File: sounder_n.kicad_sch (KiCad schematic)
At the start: 20 parts

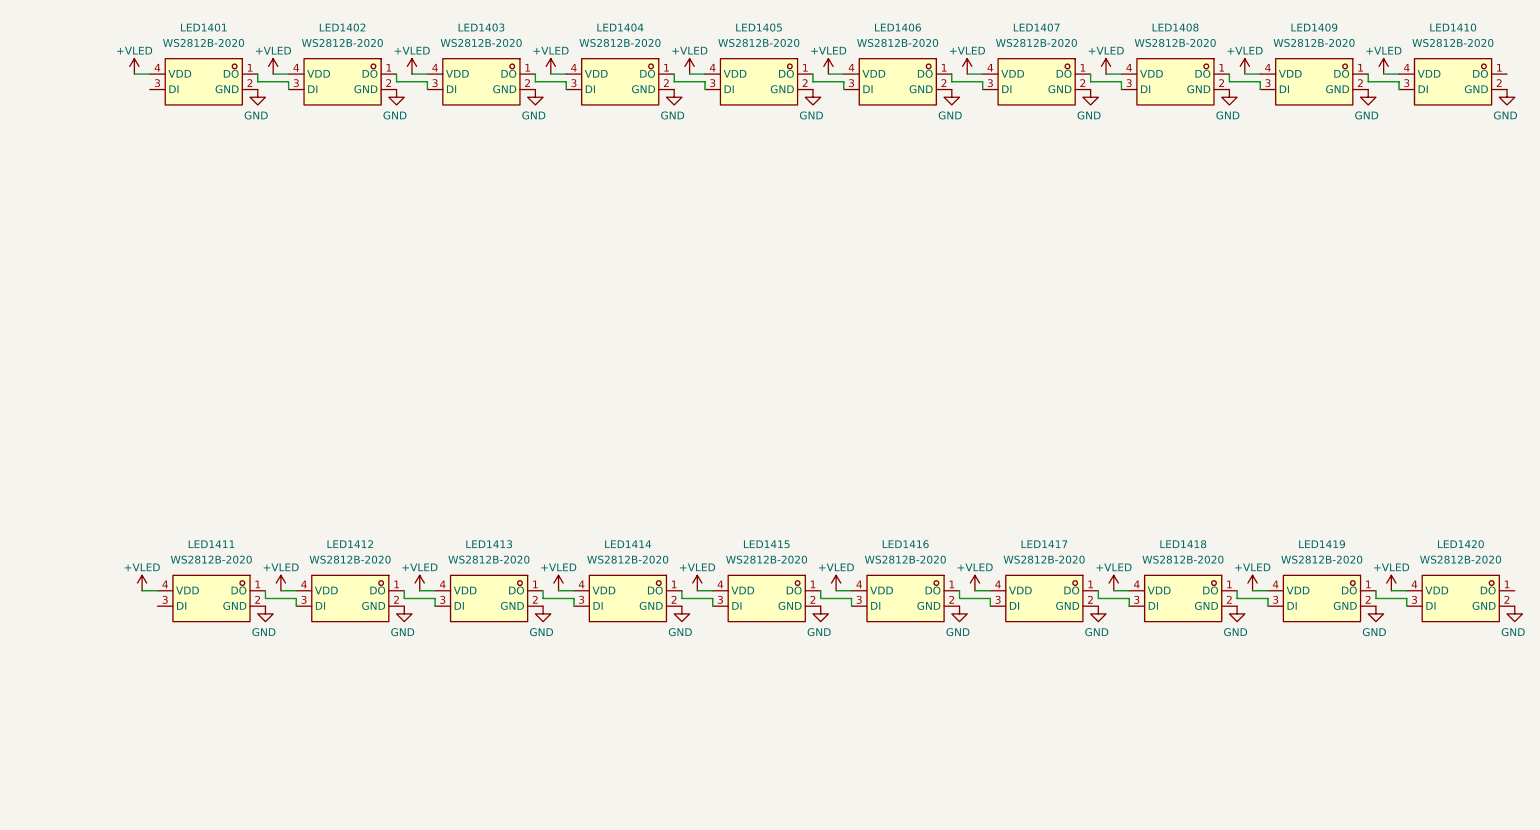
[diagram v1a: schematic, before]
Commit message: Initial LED placement complete
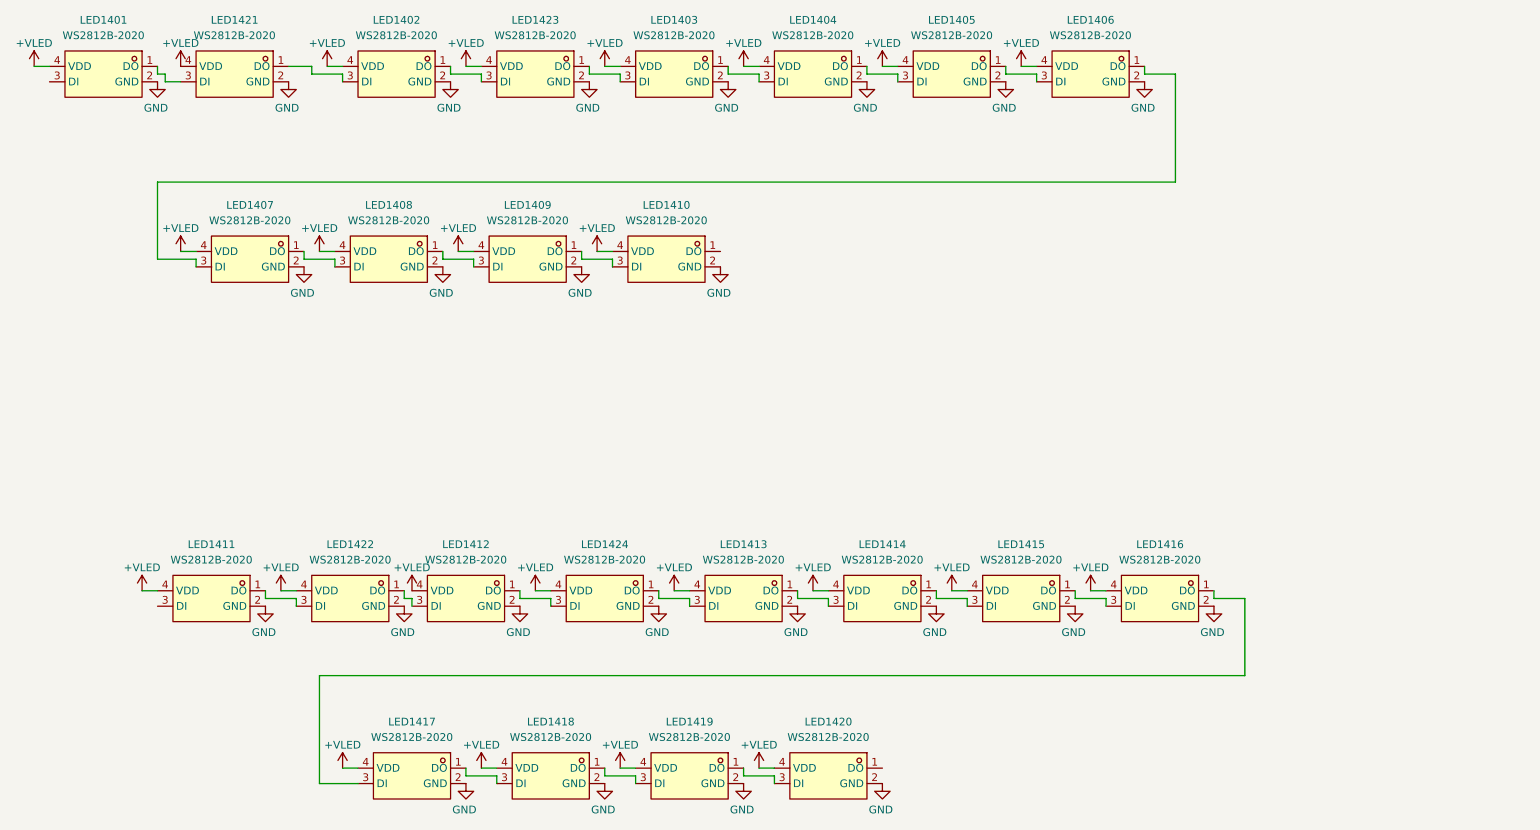
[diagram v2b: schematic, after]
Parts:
- added LED1421, LED1422, LED1423, LED1424: WS2812B-2020, EasyEDA:LED-SMD_4P-L2.0-W2.0-TL_WS2812B-2020, symbol EasyEDA:WS2812B-2020
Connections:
- net +VLED: now also LED1421.4 (VDD), LED1422.4 (VDD), LED1423.4 (VDD), LED1424.4 (VDD)
- net GND: now also LED1421.2 (GND), LED1422.2 (GND), LED1423.2 (GND), LED1424.2 (GND)
- net at LED1411.1 (DO): now also LED1422.3 (DI); no longer LED1412.3 (DI)
- net at LED1403.3 (DI): now also LED1423.1 (DO); no longer LED1402.1 (DO)
- net at LED1412.1 (DO): now also LED1424.3 (DI); no longer LED1413.3 (DI)
- net at LED1401.1 (DO): now also LED1421.3 (DI); no longer LED1402.3 (DI)
- new net: LED1412.3 (DI), LED1422.1 (DO)
- new net: LED1402.3 (DI), LED1421.1 (DO)
- new net: LED1413.3 (DI), LED1424.1 (DO)
- new net: LED1402.1 (DO), LED1423.3 (DI)
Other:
- moved on the sheet: LED1402, LED1403, LED1404, LED1405, LED1406

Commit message: Add rail labels
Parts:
- renumbered LED1421 to LED1402, LED1402 to LED1403, LED1423 to LED1404, LED1403 to LED1405, LED1404 to LED1406, LED1405 to LED1407, LED1406 to LED1408, LED1407 to LED1409, LED1408 to LED1410, LED1409 to LED1411, LED1410 to LED1412, LED1411 to LED1413, LED1422 to LED1414, LED1412 to LED1415, LED1424 to LED1416, LED1413 to LED1417, LED1414 to LED1418, LED1415 to LED1419, LED1416 to LED1420, LED1417 to LED1421, LED1418 to LED1422, LED1419 to LED1423, LED1420 to LED1424
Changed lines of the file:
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@@
 		(in_pos_files yes)
 		(dnp no)
-		(property "Reference" "LED1410"
+		(property "Reference" "LED1412"
 			(at 120.65 50.8 0)
 			(show_name no)
@@
 			(project "transit"
 				(path "/3763eade-a8c8-4ec0-9cf2-9db4442b4ee5/77ee1b5c-3800-46a1-aec6-a1e3c1d3f80f/996df8f8-04d4-4bb4-8f37-9760745edbe2"
-					(reference "LED1410")
+					(reference "LED1412")
 					(unit 1)
 				)
@@
 		(in_pos_files yes)
 		(dnp no)
-		(property "Reference" "LED1411"
+		(property "Reference" "LED1413"
 			(at 45.72 106.68 0)
 			(show_name no)
@@
 			(project "transit"
 				(path "/3763eade-a8c8-4ec0-9cf2-9db4442b4ee5/77ee1b5c-3800-46a1-aec6-a1e3c1d3f80f/996df8f8-04d4-4bb4-8f37-9760745edbe2"
-					(reference "LED1411")
+					(reference "LED1413")
 					(unit 1)
 				)
@@
 		(in_pos_files yes)
 		(dnp no)
-		(property "Reference" "LED1403"
+		(property "Reference" "LED1405"
 			(at 121.92 20.32 0)
 			(show_name no)
@@
 			(project "transit"
 				(path "/3763eade-a8c8-4ec0-9cf2-9db4442b4ee5/77ee1b5c-3800-46a1-aec6-a1e3c1d3f80f/996df8f8-04d4-4bb4-8f37-9760745edbe2"
-					(reference "LED1403")
+					(reference "LED1405")
 					(unit 1)
 				)
@@
 		(in_pos_files yes)
 		(dnp no)
-		(property "Reference" "LED1404"
+		(property "Reference" "LED1406"
 			(at 144.78 20.32 0)
 			(show_name no)
@@
 			(project "transit"
 				(path "/3763eade-a8c8-4ec0-9cf2-9db4442b4ee5/77ee1b5c-3800-46a1-aec6-a1e3c1d3f80f/996df8f8-04d4-4bb4-8f37-9760745edbe2"
-					(reference "LED1404")
+					(reference "LED1406")
 					(unit 1)
 				)
@@
 		(in_pos_files yes)
 		(dnp no)
-		(property "Reference" "LED1414"
+		(property "Reference" "LED1418"
 			(at 156.21 106.68 0)
 			(show_name no)
@@
 			(project "transit"
 				(path "/3763eade-a8c8-4ec0-9cf2-9db4442b4ee5/77ee1b5c-3800-46a1-aec6-a1e3c1d3f80f/996df8f8-04d4-4bb4-8f37-9760745edbe2"
-					(reference "LED1414")
+					(reference "LED1418")
 					(unit 1)
 				)
@@
 		(in_pos_files yes)
 		(dnp no)
-		(property "Reference" "LED1422"
+		(property "Reference" "LED1414"
 			(at 68.58 106.68 0)
 			(show_name no)
@@
 			(project "transit"
 				(path "/3763eade-a8c8-4ec0-9cf2-9db4442b4ee5/77ee1b5c-3800-46a1-aec6-a1e3c1d3f80f/996df8f8-04d4-4bb4-8f37-9760745edbe2"
-					(reference "LED1422")
+					(reference "LED1414")
 					(unit 1)
 				)
@@
 		(in_pos_files yes)
 		(dnp no)
-		(property "Reference" "LED1405"
+		(property "Reference" "LED1407"
 			(at 167.64 20.32 0)
 			(show_name no)
@@
 			(project "transit"
 				(path "/3763eade-a8c8-4ec0-9cf2-9db4442b4ee5/77ee1b5c-3800-46a1-aec6-a1e3c1d3f80f/996df8f8-04d4-4bb4-8f37-9760745edbe2"
-					(reference "LED1405")
+					(reference "LED1407")
 					(unit 1)
 				)
@@
 		(in_pos_files yes)
 		(dnp no)
-		(property "Reference" "LED1408"
+		(property "Reference" "LED1410"
 			(at 74.93 50.8 0)
 			(show_name no)
@@
 			(project "transit"
 				(path "/3763eade-a8c8-4ec0-9cf2-9db4442b4ee5/77ee1b5c-3800-46a1-aec6-a1e3c1d3f80f/996df8f8-04d4-4bb4-8f37-9760745edbe2"
-					(reference "LED1408")
+					(reference "LED1410")
 					(unit 1)
 				)
@@
 		(in_pos_files yes)
 		(dnp no)
-		(property "Reference" "LED1416"
+		(property "Reference" "LED1420"
 			(at 201.93 106.68 0)
 			(show_name no)
@@
 			(project "transit"
 				(path "/3763eade-a8c8-4ec0-9cf2-9db4442b4ee5/77ee1b5c-3800-46a1-aec6-a1e3c1d3f80f/996df8f8-04d4-4bb4-8f37-9760745edbe2"
-					(reference "LED1416")
+					(reference "LED1420")
 					(unit 1)
 				)
@@
 		(in_pos_files yes)
 		(dnp no)
-		(property "Reference" "LED1415"
+		(property "Reference" "LED1419"
 			(at 179.07 106.68 0)
 			(show_name no)
@@
 			(project "transit"
 				(path "/3763eade-a8c8-4ec0-9cf2-9db4442b4ee5/77ee1b5c-3800-46a1-aec6-a1e3c1d3f80f/996df8f8-04d4-4bb4-8f37-9760745edbe2"
-					(reference "LED1415")
+					(reference "LED1419")
 					(unit 1)
 				)
@@
 		(in_pos_files yes)
 		(dnp no)
-		(property "Reference" "LED1406"
+		(property "Reference" "LED1408"
 			(at 190.5 20.32 0)
 			(show_name no)
@@
 			(project "transit"
 				(path "/3763eade-a8c8-4ec0-9cf2-9db4442b4ee5/77ee1b5c-3800-46a1-aec6-a1e3c1d3f80f/996df8f8-04d4-4bb4-8f37-9760745edbe2"
-					(reference "LED1406")
+					(reference "LED1408")
 					(unit 1)
 				)
@@
 		(in_pos_files yes)
 		(dnp no)
-		(property "Reference" "LED1412"
+		(property "Reference" "LED1415"
 			(at 87.63 106.68 0)
 			(show_name no)
@@
 			(project "transit"
 				(path "/3763eade-a8c8-4ec0-9cf2-9db4442b4ee5/77ee1b5c-3800-46a1-aec6-a1e3c1d3f80f/996df8f8-04d4-4bb4-8f37-9760745edbe2"
-					(reference "LED1412")
+					(reference "LED1415")
 					(unit 1)
 				)
@@
 		(in_pos_files yes)
 		(dnp no)
-		(property "Reference" "LED1421"
+		(property "Reference" "LED1402"
 			(at 49.53 20.32 0)
 			(show_name no)
@@
 			(project "transit"
 				(path "/3763eade-a8c8-4ec0-9cf2-9db4442b4ee5/77ee1b5c-3800-46a1-aec6-a1e3c1d3f80f/996df8f8-04d4-4bb4-8f37-9760745edbe2"
-					(reference "LED1421")
+					(reference "LED1402")
 					(unit 1)
 				)
@@
 		(in_pos_files yes)
 		(dnp no)
-		(property "Reference" "LED1418"
+		(property "Reference" "LED1422"
 			(at 101.6 135.89 0)
 			(show_name no)
@@
 			(project "transit"
 				(path "/3763eade-a8c8-4ec0-9cf2-9db4442b4ee5/77ee1b5c-3800-46a1-aec6-a1e3c1d3f80f/996df8f8-04d4-4bb4-8f37-9760745edbe2"
-					(reference "LED1418")
+					(reference "LED1422")
 					(unit 1)
 				)
@@
 		(in_pos_files yes)
 		(dnp no)
-		(property "Reference" "LED1420"
+		(property "Reference" "LED1424"
 			(at 147.32 135.89 0)
 			(show_name no)
@@
 			(project "transit"
 				(path "/3763eade-a8c8-4ec0-9cf2-9db4442b4ee5/77ee1b5c-3800-46a1-aec6-a1e3c1d3f80f/996df8f8-04d4-4bb4-8f37-9760745edbe2"
-					(reference "LED1420")
+					(reference "LED1424")
 					(unit 1)
 				)
@@
 		(in_pos_files yes)
 		(dnp no)
-		(property "Reference" "LED1417"
+		(property "Reference" "LED1421"
 			(at 78.74 135.89 0)
 			(show_name no)
@@
 			(project "transit"
 				(path "/3763eade-a8c8-4ec0-9cf2-9db4442b4ee5/77ee1b5c-3800-46a1-aec6-a1e3c1d3f80f/996df8f8-04d4-4bb4-8f37-9760745edbe2"
-					(reference "LED1417")
+					(reference "LED1421")
 					(unit 1)
 				)
@@
 		(in_pos_files yes)
 		(dnp no)
-		(property "Reference" "LED1419"
+		(property "Reference" "LED1423"
 			(at 124.46 135.89 0)
 			(show_name no)
@@
 			(project "transit"
 				(path "/3763eade-a8c8-4ec0-9cf2-9db4442b4ee5/77ee1b5c-3800-46a1-aec6-a1e3c1d3f80f/996df8f8-04d4-4bb4-8f37-9760745edbe2"
-					(reference "LED1419")
+					(reference "LED1423")
 					(unit 1)
 				)
@@
 		(in_pos_files yes)
 		(dnp no)
-		(property "Reference" "LED1413"
+		(property "Reference" "LED1417"
 			(at 133.35 106.68 0)
 			(show_name no)
@@
 			(project "transit"
 				(path "/3763eade-a8c8-4ec0-9cf2-9db4442b4ee5/77ee1b5c-3800-46a1-aec6-a1e3c1d3f80f/996df8f8-04d4-4bb4-8f37-9760745edbe2"
-					(reference "LED1413")
+					(reference "LED1417")
 					(unit 1)
 				)
@@
 		(in_pos_files yes)
 		(dnp no)
-		(property "Reference" "LED1407"
+		(property "Reference" "LED1409"
 			(at 52.07 50.8 0)
 			(show_name no)
@@
 			(project "transit"
 				(path "/3763eade-a8c8-4ec0-9cf2-9db4442b4ee5/77ee1b5c-3800-46a1-aec6-a1e3c1d3f80f/996df8f8-04d4-4bb4-8f37-9760745edbe2"
-					(reference "LED1407")
+					(reference "LED1409")
 					(unit 1)
 				)
@@
 		(in_pos_files yes)
 		(dnp no)
-		(property "Reference" "LED1409"
+		(property "Reference" "LED1411"
 			(at 97.79 50.8 0)
 			(show_name no)
@@
 			(project "transit"
 				(path "/3763eade-a8c8-4ec0-9cf2-9db4442b4ee5/77ee1b5c-3800-46a1-aec6-a1e3c1d3f80f/996df8f8-04d4-4bb4-8f37-9760745edbe2"
-					(reference "LED1409")
+					(reference "LED1411")
 					(unit 1)
 				)
@@
 		(in_pos_files yes)
 		(dnp no)
-		(property "Reference" "LED1402"
+		(property "Reference" "LED1403"
 			(at 76.2 20.32 0)
 			(show_name no)
@@
 			(project "transit"
 				(path "/3763eade-a8c8-4ec0-9cf2-9db4442b4ee5/77ee1b5c-3800-46a1-aec6-a1e3c1d3f80f/996df8f8-04d4-4bb4-8f37-9760745edbe2"
-					(reference "LED1402")
+					(reference "LED1403")
 					(unit 1)
 				)
@@
 		(in_pos_files yes)
 		(dnp no)
-		(property "Reference" "LED1423"
+		(property "Reference" "LED1404"
 			(at 99.06 20.32 0)
 			(show_name no)
@@
 			(project "transit"
 				(path "/3763eade-a8c8-4ec0-9cf2-9db4442b4ee5/77ee1b5c-3800-46a1-aec6-a1e3c1d3f80f/996df8f8-04d4-4bb4-8f37-9760745edbe2"
-					(reference "LED1423")
+					(reference "LED1404")
 					(unit 1)
 				)
@@
 		(in_pos_files yes)
 		(dnp no)
-		(property "Reference" "LED1424"
+		(property "Reference" "LED1416"
 			(at 110.49 106.68 0)
 			(show_name no)
@@
 			(project "transit"
 				(path "/3763eade-a8c8-4ec0-9cf2-9db4442b4ee5/77ee1b5c-3800-46a1-aec6-a1e3c1d3f80f/996df8f8-04d4-4bb4-8f37-9760745edbe2"
-					(reference "LED1424")
+					(reference "LED1416")
 					(unit 1)
 				)

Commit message: Renumber Sounder, ready to route
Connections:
- net at LED1412.1 (DO): now also LED1413.3 (DI)
- net SOUNDER_S_N: now reaches LED1401.3 (DI)
- net SOUNDER_N_S: now reaches LED1424.1 (DO)
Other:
- moved on the sheet: LED1401, LED1402, LED1403, LED1404, LED1405, LED1406, LED1407, LED1408, LED1409, LED1410, LED1411, LED1412
